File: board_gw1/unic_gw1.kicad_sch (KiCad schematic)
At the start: 127 parts, among them Q1 2N7002, Q10 2N7002, Q11 2N7002, Q12 2N7002, Q13 2N7002, Q14 2N7002, Q15 2N7002, Q16 2N7002, Q17 2N7002, Q18 2N7002, Q19 2N7002, Q2 2N7002, Q20 2N7002, Q21 2N7002, Q22 2N7002, Q23 2N7002, Q24 2N7002, Q25 2N7002, Q26 2N7002, Q27 2N7002, Q28 2N7002, Q29 2N7002, Q3 2N7002, Q30 2N7002, Q31 2N7002, Q32 2N7002, Q33 2N7002, Q34 2N7002, Q35 2N7002, Q36 2N7002, Q37 2N7002, Q38 2N7002, Q39 2N7002, Q4 2N7002, Q40 2N7002, Q41 2N7002, Q5 2N7002, Q6 2N7002, Q7 2N7002, Q8 2N7002, Q9 2N7002, U1 GW1NR-LV9-QN88-C6/I5, U3 MIC5203-3.3BM5, U4 APS6404L-3SQR-ZR, U5 MIC5504-1.2YM5, U6 AP62150Z6, U7 W25Q16JVUXIQ, X1 27MHz

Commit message: New diodes are added
PCB is also fixed up, but fab notes
need cleaning. Also, I need to select
an actual diode.
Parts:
- removed D1, D11, D2, D3, D4, D5, D6, D7, D8, D9: BAT54DF, UNIC:SOT65P210X110-6N, symbol UNIC:BAT54DF
- removed D21, D22, D23, D24, D25, D26, D27, D28, D29, D30: BAT54CV, UNIC:SOT-666, symbol UNIC:BAT54CV
- added D1, D10, D11, D12, D13, D14, D15, D16, D17, D18, D19, D2, D20, D3, D31, D32, D33, D34, D35, D36, D37, D38, D39, D4, D40, D41, D42, D43, D44, D45, D46, D47, D48, D49, D5, D50, D51, D52, D53, D54, D55, D56, D57, D58, D59, D6, D60, D61, D62, D63, D64, D65, D66, D67, D68, D69, D7, D70, D71, D72, D73, D74, D75, D76, D77, D78, D79, D8, D80, D81, D82, D83, D84, D85, D86, D87, D88, D89, D9, D90: D_Schottky, Diode_SMD:D_SOD-882, symbol Device:D_Schottky
- added TP5: TestPoint, UNIC:TestPoint_Pad_D2.0mm, symbol Connector:TestPoint
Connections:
- net GND: now also D10.2 (A), D11.2 (A), D13.2 (A), D15.2 (A), D17.2 (A), D19.2 (A), D3.2 (A), D31.2 (A), D33.2 (A), D35.2 (A), D37.2 (A), D39.2 (A), D41.2 (A), D42.2 (A), D44.2 (A), D46.2 (A), D48.2 (A), D50.2 (A), D52.2 (A), D54.2 (A), D56.2 (A), D58.2 (A), D6.2 (A), D60.2 (A), D62.2 (A), D64.2 (A), D66.2 (A), D68.2 (A), D70.2 (A), D72.2 (A), D74.2 (A), D76.2 (A), D78.2 (A), D8.2 (A), D80.2 (A), D82.2 (A), D84.2 (A), D86.2 (A), D88.2 (A), D90.2 (A), TP5.1
- net LINE: now also D1.1 (K), D12.1 (K), D14.1 (K), D16.1 (K), D18.1 (K), D2.1 (K), D20.1 (K), D32.1 (K), D34.1 (K), D36.1 (K), D38.1 (K), D4.1 (K), D40.1 (K), D43.1 (K), D45.1 (K), D47.1 (K), D49.1 (K), D5.1 (K), D51.1 (K), D53.1 (K), D55.1 (K), D57.1 (K), D59.1 (K), D61.1 (K), D63.1 (K), D65.1 (K), D67.1 (K), D69.1 (K), D7.1 (K), D71.1 (K), D73.1 (K), D75.1 (K), D77.1 (K), D79.1 (K), D81.1 (K), D83.1 (K), D85.1 (K), D87.1 (K), D89.1 (K), D9.1 (K)
- net PIN1: now also D2.2 (A), D3.1 (K)
- net PIN10: now also D34.2 (A), D35.1 (K)
- net PIN11: now also D16.2 (A), D17.1 (K)
- net PIN12: now also D45.2 (A), D46.1 (K)
- net PIN13: now also D18.2 (A), D19.1 (K)
- net PIN14: now also D40.2 (A), D41.1 (K)
- net PIN15: now also D4.2 (A), D6.1 (K)
- net PIN16: now also D71.2 (A), D72.1 (K)
- net PIN17: now also D61.2 (A), D62.1 (K)
- net PIN18: now also D55.2 (A), D56.1 (K)
- net PIN19: now also D32.2 (A), D33.1 (K)
- net PIN2: now also D57.2 (A), D58.1 (K)
- net PIN20: now also D20.2 (A), D31.1 (K)
- net PIN21: now also D38.2 (A), D39.1 (K)
- net PIN22: now also D7.2 (A), D8.1 (K)
- net PIN23: now also D75.2 (A), D76.1 (K)
- net PIN24: now also D69.2 (A), D70.1 (K)
- net PIN25: now also D63.2 (A), D64.1 (K)
- net PIN26: now also D11.1 (K), D9.2 (A)
- net PIN27: now also D83.2 (A), D84.1 (K)
- net PIN28: now also D47.2 (A), D48.1 (K)
- net PIN29: now also D85.2 (A), D86.1 (K)
- net PIN3: now also D43.2 (A), D44.1 (K)
- net PIN30: now also D53.2 (A), D54.1 (K)
- net PIN31: now also D87.2 (A), D88.1 (K)
- net PIN32: now also D36.2 (A), D37.1 (K)
- net PIN33: now also D67.2 (A), D68.1 (K)
- net PIN34: now also D65.2 (A), D66.1 (K)
- net PIN35: now also D51.2 (A), D52.1 (K)
- net PIN36: now also D49.2 (A), D50.1 (K)
- net PIN37: now also D81.2 (A), D82.1 (K)
- net PIN38: now also D79.2 (A), D80.1 (K)
- net PIN39: now also D77.2 (A), D78.1 (K)
- net PIN4: now also D1.2 (A), D42.1 (K)
- net PIN40: now also D89.2 (A), D90.1 (K)
- net PIN5: now also D13.1 (K), D5.2 (A)
- net PIN6: now also D14.2 (A), D15.1 (K)
- net PIN7: now also D73.2 (A), D74.1 (K)
- net PIN8: now also D59.2 (A), D60.1 (K)
- net PIN9: now also D10.1 (K), D12.2 (A)

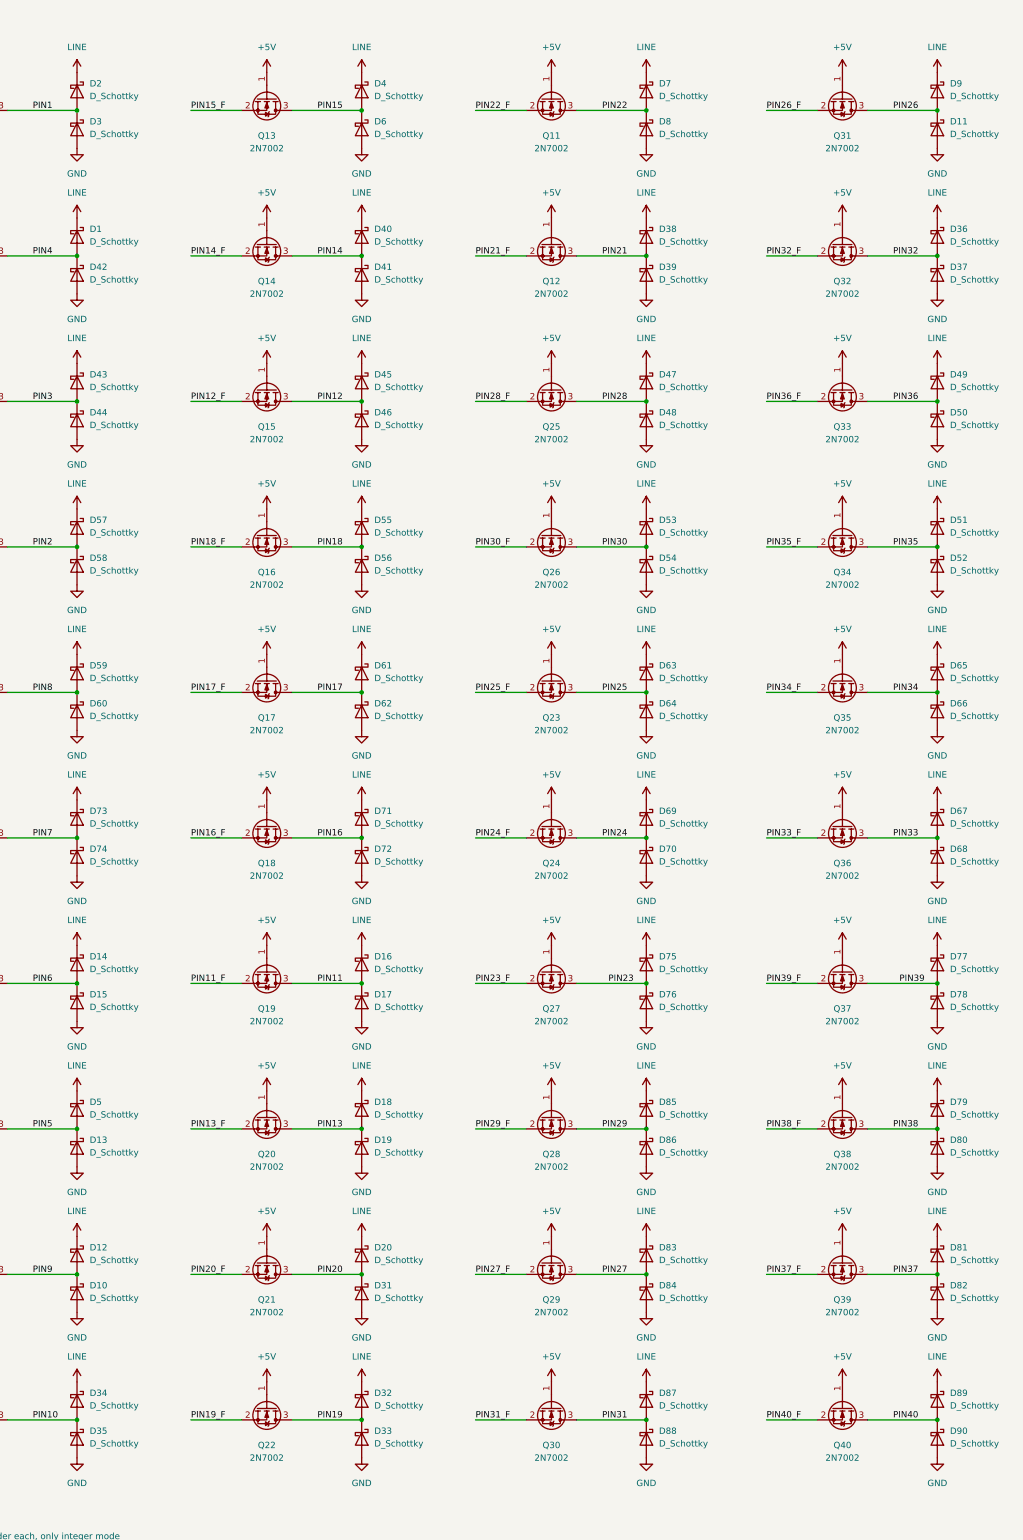
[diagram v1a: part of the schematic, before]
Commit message: Updated diode part and footprint.
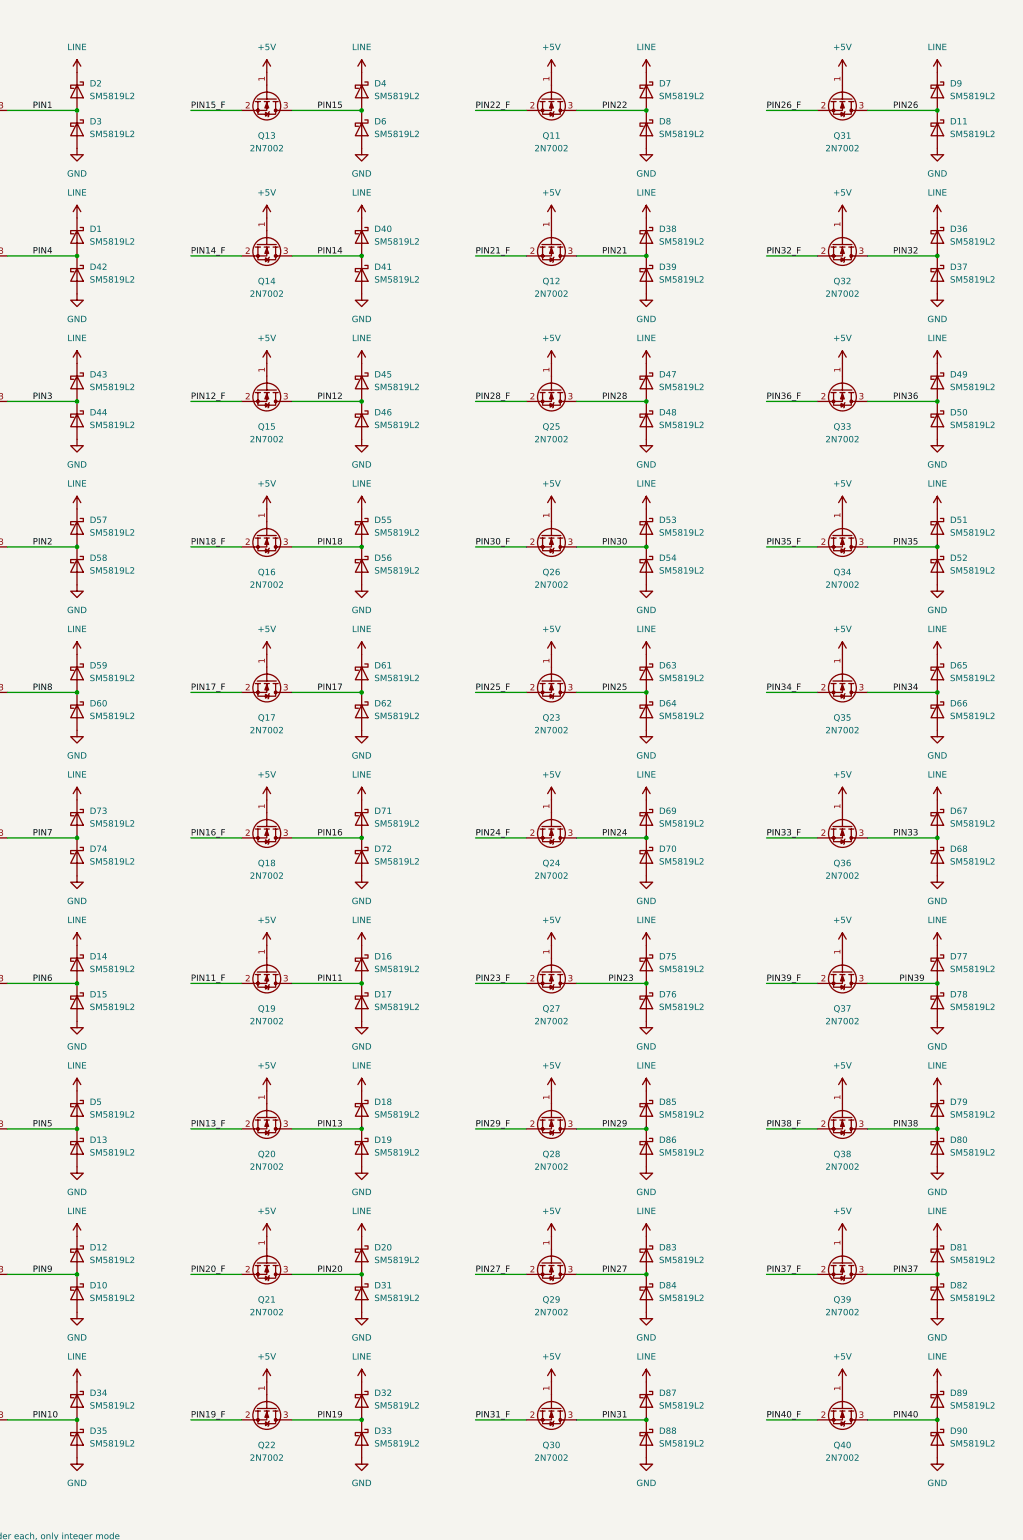
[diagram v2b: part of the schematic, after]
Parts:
- D1, D10, D11, D12, D13, D14, D15, D16, D17, D18, D19, D2, D20, D3, D31, D32, D33, D34, D35, D36, D37, D38, D39, D4, D40, D41, D42, D43, D44, D45, D46, D47, D48, D49, D5, D50, D51, D52, D53, D54, D55, D56, D57, D58, D59, D6, D60, D61, D62, D63, D64, D65, D66, D67, D68, D69, D7, D70, D71, D72, D73, D74, D75, D76, D77, D78, D79, D8, D80, D81, D82, D83, D84, D85, D86, D87, D88, D89, D9, D90: value D_Schottky -> SM5819L2; footprint Diode_SMD:D_SOD-882 -> UNIC:D_SOD-882

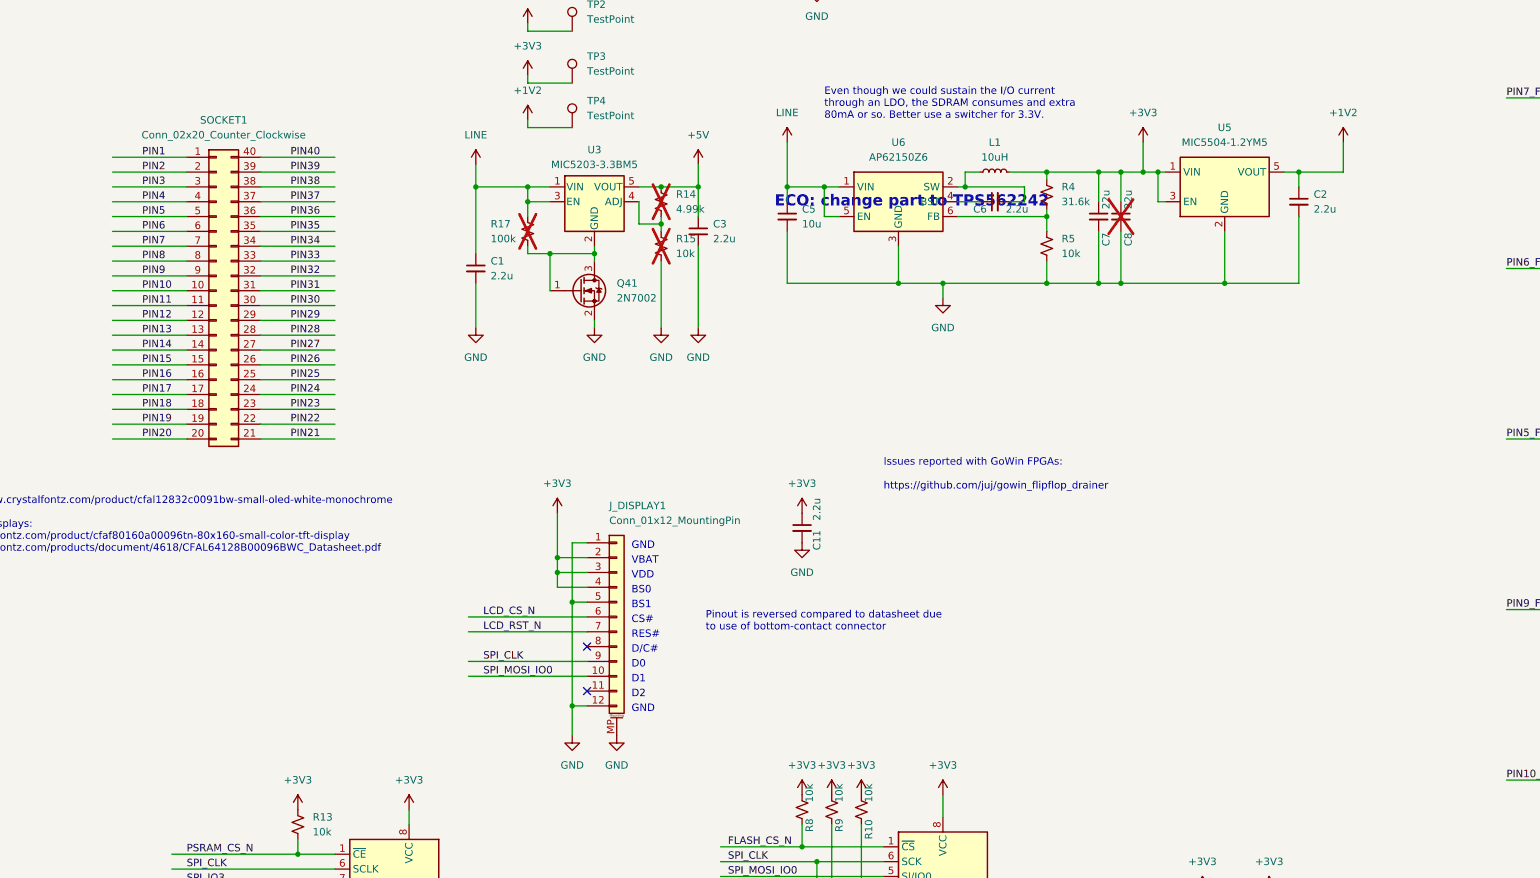
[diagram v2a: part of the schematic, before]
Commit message: Brought UnIC  V1 up to date with latest changes.
Updated OLED display connector and pinout
Added DC/DC 33pF cap
Added keepouts on bottom side for case clamps
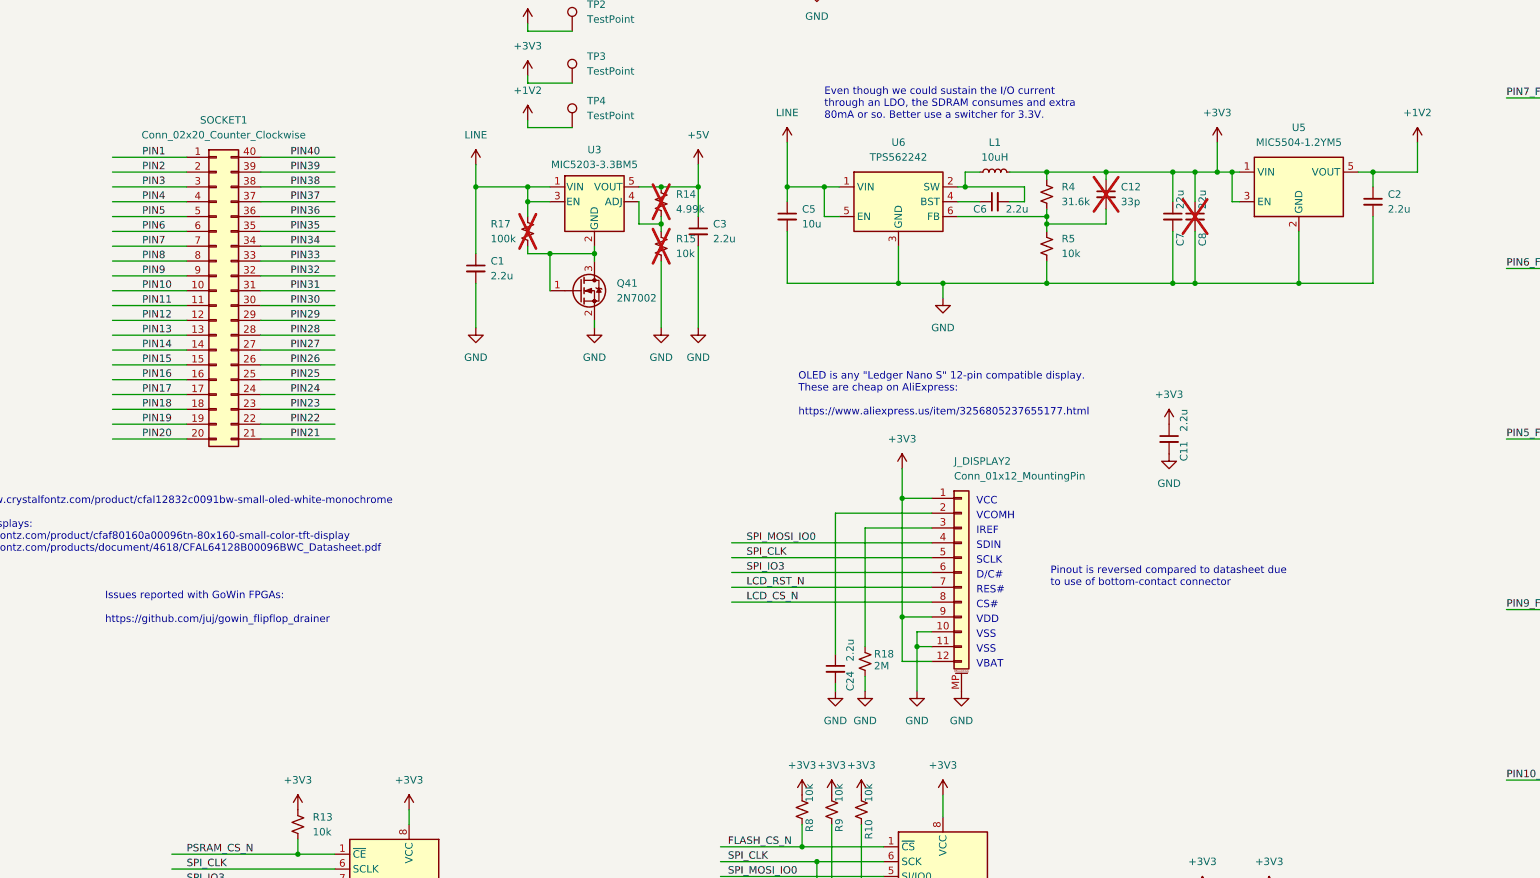
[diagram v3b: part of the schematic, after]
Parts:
- removed J_DISPLAY1: Conn_01x12_MountingPin, UNIC:CF31121D0R0-05-NH, symbol Connector_Generic_MountingPin:Conn_01x12_MountingPin
- added C12: 33p, UNIC:C_0402_1005Metric_Pad0.74x0.62mm_HandSolder, symbol Device:C_Small
- added C24: 2.2u, UNIC:C_0402_1005Metric_Pad0.74x0.62mm_HandSolder, symbol Device:C_Small
- added J_DISPLAY2: Conn_01x12_MountingPin, UNIC:CF4212FH0R0-05-NH, symbol Connector_Generic_MountingPin:Conn_01x12_MountingPin
- added R18: 2M, UNIC:R_0402_1005Metric_Pad0.72x0.64mm_HandSolder, symbol Device:R_Small_US
- U6: value AP62150Z6 -> TPS562242; manufacturer Diodes Incorporated -> Texas Instruments; mpn AP62150Z6-7 -> TPS562242
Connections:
- net +3V3: now also C12.1, J_DISPLAY2.1 (Pin_1), J_DISPLAY2.12 (Pin_12), J_DISPLAY2.9 (Pin_9)
- net GND: now also C24.2, J_DISPLAY2.10 (Pin_10), J_DISPLAY2.11 (Pin_11), J_DISPLAY2.MP (MountPin), R18.2
- net LCD_CS_N: now also J_DISPLAY2.8 (Pin_8)
- net LCD_RST_N: now also J_DISPLAY2.7 (Pin_7)
- net SPI_CLK: now also J_DISPLAY2.5 (Pin_5)
- net SPI_IO3: now also J_DISPLAY2.6 (Pin_6)
- net SPI_MOSI_IO0: now also J_DISPLAY2.4 (Pin_4)
- net at R4.2, R5.1, U6.6 (FB): now also C12.2
- new net: J_DISPLAY2.3 (Pin_3), R18.1
- new net: C24.1, J_DISPLAY2.2 (Pin_2)
- no-connect marks 3 -> 1
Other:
- note added: "IREF"
- note added: "OLED is any "Ledger Nano S" 12-pin compatible display. These are cheap on AliExpress: https://www.aliexpress.us/item/3256805237655177.html"
- note added: "SCLK"
- note added: "SDIN"
- note added: "VCC"
- note added: "VCOMH"
- note added: "VSS"
- note removed: "BS0"
- note removed: "BS1"
- note removed: "D0"
- note removed: "D1"
- note removed: "D2"
- note removed: "ECO: change part to TPS562242"
- note removed: "GND"
- moved on the sheet: C11, C2, C7, C8, U5
